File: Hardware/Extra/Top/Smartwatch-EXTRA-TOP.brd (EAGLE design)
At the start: 38 x 38 mm, 69 parts, among them SW6 SWITCH.MOM, SW7 SWITCH.MOM, U2 NRF52832_MODULE_MDBT42, U4 FT231XS, U5 PHOTOTRANSISTOR

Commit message: Extra features updated
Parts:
- removed C25: 1u, LinnesLab-Passives:C0603
- removed C26: 100n, LinnesLab-Passives:C0603
- removed D4: (no value), LinnesLab-DiscreteSemi:USC
- removed LED5: RED, LinnesLab-LED:LED-0603
- removed LED6: YELLOW, LinnesLab-LED:LED-0603
- removed Q1: (no value), LinnesLab-DiscreteSemi:SOT23-3
- removed R17: 1k, LinnesLab-Passives:R0603
- removed SW6, SW7: SWITCH.MOM, LinnesLab-Switches:TACTILE_SWITCH_SMD_6.2MM_TALL
- removed U4: FT231XS, LinnesLab-DigitalIC:SSOP20_L
- added C2: 10u, LinnesLab-Passives:C0805
- added C27: 10p, LinnesLab-Passives:C0603
- added C28: 1u, LinnesLab-Passives:C0603
- added C29: 100n, LinnesLab-Passives:C0603
- added D3: (no value), LinnesLab-DiscreteSemi:USC
- added J3: (no value), LinnesLab-Connectors:1X04_1.27MM
- added LED1: RED, LinnesLab-LED:LED-0603
- added LED2: BLUE, LinnesLab-LED:LED-0603
- added MIC1: (no value), LinnesLab-Electromechanical:MICROPHONE_CMEJ-0415-42-P
- added Q2: (no value), LinnesLab-DiscreteSemi:SOT23-3@1
- added Q3: (no value), LinnesLab-DiscreteSemi:SOT23-3
- added R21: 100k, LinnesLab-Passives:R0603
- added R22, R23, R26: 10k, LinnesLab-Passives:R0603
- added R9: 27, LinnesLab-Passives:R0603
- added U1: NRF52832_MODULE_MDBT42, LinnesLab-Microcontrollers:BLE_MODULE_RAYTAC_MDBT42
- added U6: MCP9808-MSOP8, LinnesLab-Sensors:MSOP08
- C1: value 4.7u -> 1u
- C10, C11: value 300p -> 2.2uF; device LinnesLab-Passives:C0603 -> LinnesLab-Passives:C0402
- C12: value 10u -> 2.2uF; device LinnesLab-Passives:C0805 -> LinnesLab-Passives:C0402
- C13, C18: value 2.2uF -> 100n; device LinnesLab-Passives:C0402 -> LinnesLab-Passives:C0603
- C14: value 100n -> 4.7u
- C15, C17: value 2.2uF -> 47p; device LinnesLab-Passives:C0402 -> LinnesLab-Passives:C0603
- C16: value 10uF -> 1u
- C19: value 2.2uF -> 1u; device LinnesLab-Passives:C0402 -> LinnesLab-Passives:C0603
- C20: value 2.2u -> 4.7u
- C22: value 47p -> 2.2u
- C23: value 47p -> 100n
- C24: value 10p -> 100n
- C3: value 4.7u -> (none)
- C4: value 100n -> (none)
- C5, C6: value 1u -> 300p
- C7: value 1u -> 10uF
- C8, C9: value (none) -> 2.2uF; device LinnesLab-Passives:C0603 -> LinnesLab-Passives:C0402
- J1: device LinnesLab-Connectors:1X07 -> LinnesLab-Connectors:1X07_1.27MM
- LED4: value BLUE -> YELLOW
- R11: value (none) -> 4.7k
- R15: value 10k -> 1k
- R16: value 27 -> 1k
- R18: value 1k -> 10k
- R6: value 10k -> 390k
- R7: value 390k -> 10k
- U2: value NRF52832_MODULE_MDBT42 -> (none); device LinnesLab-Microcontrollers:BLE_MODULE_RAYTAC_MDBT42 -> LinnesLab-Displays:UG-2864HSWEG01_0.96IN_NO-WRAPAROUND
- U3: value (none) -> FT231XS; device LinnesLab-Displays:UG-2864HSWEG01_0.96IN_NO-WRAPAROUND -> LinnesLab-DigitalIC:SSOP20_L
- moved R19 35.7 mm to (35.6, 8.17)
- moved LED4 35.1 mm to (4.55, 4.29)
- moved C11 33.2 mm to (2.93, 2.28), turned to 90 degrees
- moved U5 32.2 mm to (28.2, 7.97), turned to 270 degrees
- moved C12 29.9 mm to (1.61, 2.30)
- moved R8 28.9 mm to (2.64, 22.0), turned to 0 degrees
- moved C22 28.0 mm to (31.9, 8.10), turned to 90 degrees
- moved C5 27.7 mm to (30.9, 13.1)
- moved C19 27.6 mm to (5.81, 29.8)
- moved C14 27.1 mm to (6.17, 17.5), turned to 90 degrees
- moved C16 26.2 mm to (5.95, 25.1), turned to 270 degrees
- moved C13 24.1 mm to (33.8, 13.4), turned to 0 degrees
- moved D5 23.7 mm to (30.4, 9.48), turned to 0 degrees
- moved R18 23.6 mm to (30.2, 7.99), turned to 270 degrees
- moved C3 22.9 mm to (25.7, 15.9), turned to 180 degrees
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- renumbered CHRG2 to CHRG1, CORTEX1 to DEBUG1, JP2 to JP1, L2 to L1, LDO2 to LDO1, SW3 to SW1, USB2 to USB1, XTAL2 to XTAL1
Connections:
- removed net A0/LIGHT: C20.1, R19.2, U2.15, U5.2
- removed net D11/SW1: SW7.A1, U2.25
- removed net D15/SW2: SW6.A1, U2.29
- removed net D29/LED.CTRL: J1.6, U2.6
- removed net D5/MOTOR: Q1.1, R15.2, U2.18
- removed net N$21: SW7.B1, SW7.B2
- removed net N$22: SW6.B1, SW6.B2
- new net A0/MICROPHONE: Q2.3, R21.2, R22.1, U1.15
- new net A5/LIGHT: C22.1, R18.2, U1.6, U5.2
- new net ALERT: R26.1, U6.3
- new net D11/MOTOR: Q3.1, R19.2, U1.25
- new net D15/LED.CTRL: J1.6, U1.29
- new net D5/CD1: U1.18
- new net N$19: C23.1, MIC1.+, R23.1
- new net N$20: C23.2, Q2.1, R21.1
- net !CTS: now also U3.9; no longer U4.9
- net !DTR: now also U3.1; no longer U4.1
- net 3.3V: now also C11.2, C18.2, C19.1, C2.2, C24.1, C27.2, C28.1, C29.1, D5.-, J3.2, LED3.A, LED4.A, R12.2, R22.2, R23.2, R26.2, R7.2, U1.11, U2.6, U2.9, U3.14, U3.3, U6.8; no longer C17.2, C19.2, C24.2, C25.1, C26.1, C4.2, C6.1, D2.-, LED5.A, LED6.A, R5.2, R8.2, U2.11, U3.6, U3.9, U4.14, U4.3
- net A4/BATT: now also U1.5; no longer U2.5
- net A6/TIA: now also U1.7; no longer U2.7
- net A7/PPG: now also U1.8; no longer U2.8
- net D16/CS.OLED: now also U1.30, U2.13; no longer U2.30, U3.13
- net D27/CHRG.STAT: now also R8.1, U1.4; no longer R12.1, U2.4
- net D3/RESET.OLED: now also U1.16, U2.14; no longer U2.16, U3.14
- net D4/DC.OLED: now also U1.17, U2.15; no longer U2.17, U3.15
- net D7/SD.CS: now also U1.20; no longer U2.20
- net DFU: now also U1.34; no longer U2.34
- net DTR: now also C13.1; no longer C14.1
- net FRST: now also U1.38; no longer U2.38
- net FT3V3: now also U3.13; no longer U4.13
- net GND: now also C1.2, C11.1, C14.1, C15.1, C17.2, C19.2, C2.1, C24.2, C28.2, C29.2, C3.1, C4.2, C5.2, C7.1, C9.1, J3.1, LED1.C, LED2.C, MIC1.-, Q2.2, Q3.2, R12.1, R18.1, R5.1, R6.2, U1.1, U1.12, U1.24, U1.39, U2.10, U2.29, U2.30, U2.8, U3.16, U3.6, U6.4, U6.5, U6.6, U6.7; no longer C1.1, C10.2, C11.2, C17.1, C19.1, C23.1, C25.2, C26.2, C3.2, C4.1, C5.1, C7.2, C8.1, C9.2, LED3.C, LED4.C, Q1.2, R15.1, R6.1, R7.2, R8.1, U2.24, U2.39, U3.1, U3.10, U3.12, U3.29, U3.30, U3.8, U4.16, U4.6
- net LED1: now also U1.31; no longer U2.31
- net LED2: now also U1.33; no longer U2.33
- net MISO: now also U1.28; no longer U2.28
- net MOSI: now also U1.27, U2.19; no longer U2.27, U3.19
- net N$1: now also R5.2, U2.11; no longer R6.2, U3.11
- net N$10: now also LED2.A; no longer LED4.A
- net N$11: now also U1.10; no longer U2.10
- net N$12: now also C1.1, U1.9; no longer C7.1, U2.9
- net N$13: now also C7.2, U2.28; no longer C16.2, U3.28
- net N$15: now also C9.2, U2.27; no longer C18.2, U3.27
- net N$18: now also C27.1, D5.+, Q3.3; no longer C24.1, D2.+, Q1.3
- net N$2: now also R6.1, U2.26; no longer R7.1, U3.26
- net N$25: now also R9.2, U3.12; no longer R10.2, U4.12
- net N$26: now also R10.2, U3.11; no longer R16.2, U4.11
- net N$27: now also LED3.C, R15.2; no longer LED5.C, R17.2
- net N$28: now also LED4.C, R16.2; no longer LED6.C, R18.2
- net N$3: now also C10.2, U2.2; no longer C13.2, U3.2
- net N$4: now also C3.2, U1.13; no longer C8.2, U2.13
- net N$5: now also C10.1, U2.3; no longer C13.1, U3.3
- net N$6: now also C4.1, U1.14; no longer C9.1, U2.14
- net N$7: now also C8.2, U2.4; no longer C15.2, U3.4
- net N$8: now also C8.1, U2.5; no longer C15.1, U3.5
- net N$9: now also LED1.A; no longer LED3.A
- net P0.09/NFC1: now also C5.1, U1.22; no longer C11.1, U2.22
- net P0.10/NFC2: now also C6.1, U1.23; no longer C10.1, U2.23
- net RESET: now also C13.2, R7.1, U1.35; no longer C14.2, R5.1, U2.35
- net RXD: now also U1.21, U3.4; no longer U2.21, U4.4
- net RXLED: now also R15.1, U3.17; no longer R17.1, U4.17
- net SCK: now also U1.26, U2.18; no longer U2.26, U3.18
- net SCL: now also J3.3, U1.3, U6.2; no longer U2.3
- net SDA: now also J3.4, U1.2, U6.1; no longer U2.2
- net SWCLK: now also U1.36; no longer U2.36
- net SWDIO: now also U1.37; no longer U2.37
- net SWO: now also U1.32; no longer U2.32
- net TXD: now also U1.19, U3.20; no longer U2.19, U4.20
- net TXLED: now also R16.1, U3.10; no longer R18.1, U4.10
- net USB+: now also C17.1, R10.1; no longer C22.1, R16.1
- net USB-: now also C15.2, R9.1; no longer C23.2, R10.1
- net VIN: now also C14.2, C16.2, D2.-, D3.-, R8.2; no longer C1.2, C5.2, D4.-, D5.-, R12.2
- net VLIPO: now also C20.1, D2.+; no longer C3.1, D4.+
- net V_USB: now also D3.+, U3.15; no longer D5.+, U4.15
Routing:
- net A0/LIGHT: track 39.4 -> 0.00 mm, vias 2 -> 0
- net A0/MICROPHONE: track 0.00 -> 37.3 mm, vias 0 -> 2
- net A5/LIGHT: track 0.00 -> 37.2 mm, vias 0 -> 2
- net SCL: track 17.2 -> 48.2 mm, vias 0 -> 2
- net SDA: track 21.2 -> 49.5 mm, vias 0 -> 5
- net D15/LED.CTRL: track 0.00 -> 25.5 mm, vias 0 -> 2
- net D15/SW2: track 24.4 -> 0.00 mm, vias 2 -> 0
- net D11/SW1: track 23.0 -> 0.00 mm, vias 2 -> 0
- net D5/MOTOR: track 18.9 -> 0.00 mm, vias 2 -> 0
- net D11/MOTOR: track 0.00 -> 17.0 mm, vias 0 -> 1
- net D29/LED.CTRL: track 11.0 -> 0.00 mm
- net N$22: track 7.95 -> 0.00 mm
- net N$21: track 7.95 -> 0.00 mm
- net A6/TIA: track 16.5 -> 23.7 mm, vias 0 -> 2
- net GND: track 93.4 -> 86.2 mm, vias 30 -> 32
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
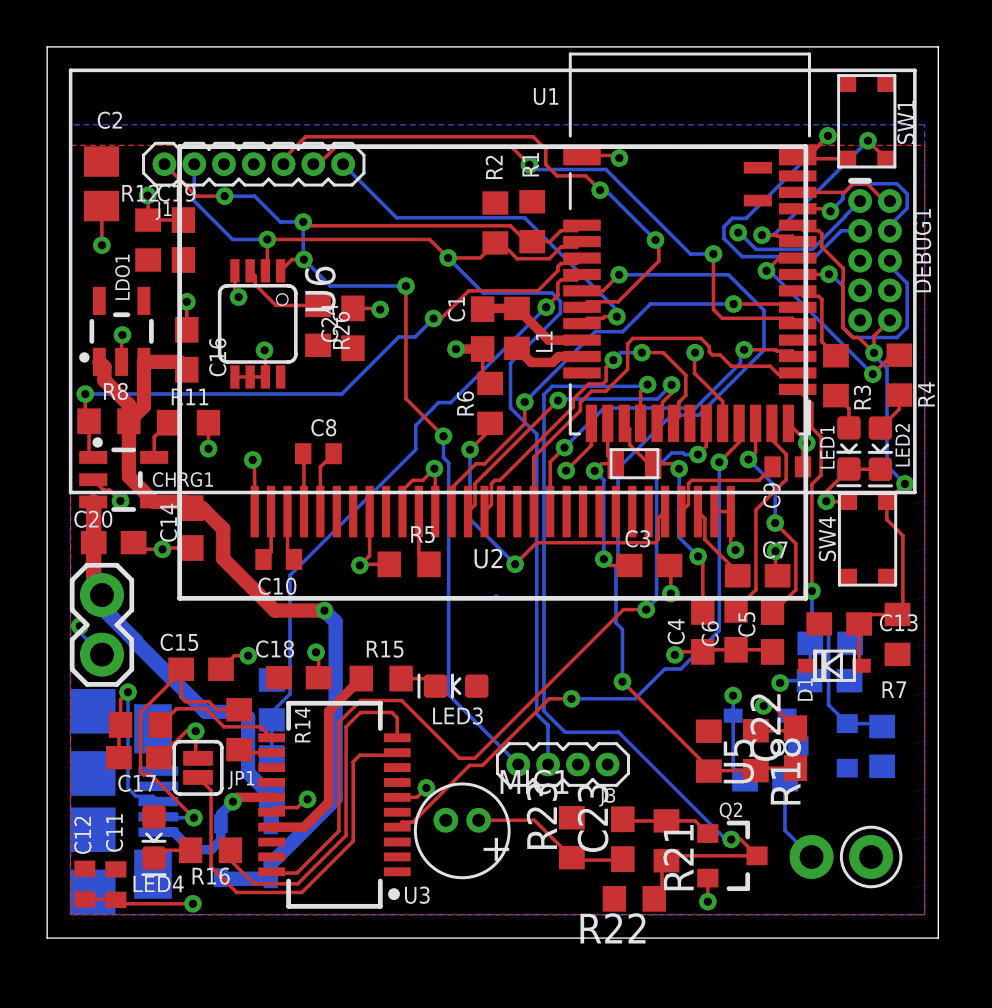
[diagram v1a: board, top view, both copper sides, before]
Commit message: Extra Silkscreens updated
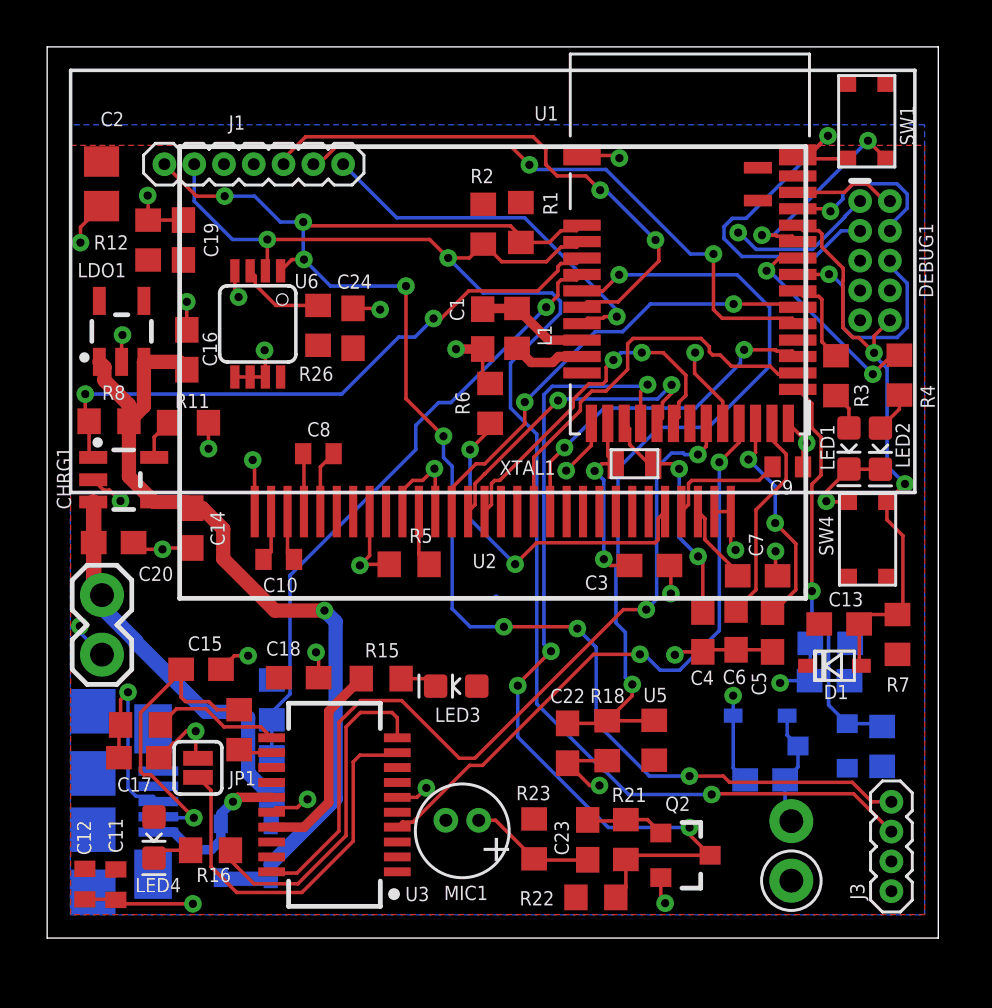
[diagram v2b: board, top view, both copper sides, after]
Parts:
- moved J3 13.3 mm to (36.0, 2.00), turned to 90 degrees
- moved C22 9.72 mm to (22.2, 8.31), turned to 270 degrees
- moved R18 6.35 mm to (23.9, 8.41), turned to 90 degrees
- moved U5 2.38 mm to (25.9, 8.43), turned to 90 degrees
- moved M1 2.15 mm to (31.7, 3.72), turned to 90 degrees
- moved Q2 2.00 mm to (27.2, 3.53)
- moved R21 1.74 mm to (24.7, 4.20)
- moved R22 1.64 mm to (23.4, 1.73)
- moved R23 1.61 mm to (20.8, 4.23)
- moved C23 1.50 mm to (23.1, 4.19)
- moved R2 0.52 mm to (18.6, 30.4)
- moved R1 0.48 mm to (20.2, 30.5)
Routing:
- net SDA: track 49.5 -> 65.9 mm, vias 5 -> 8
- net SCL: track 48.2 -> 62.9 mm, vias 2 -> 3
- net A5/LIGHT: track 37.2 -> 34.9 mm
- net N$18: track 6.92 -> 5.03 mm
- net N$19: track 6.95 -> 5.38 mm
- net RXD: track 26.4 -> 27.0 mm
- net A0/MICROPHONE: track 37.3 -> 37.6 mm, vias 2 -> 4

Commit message: Microphone Removed,Silkscreen Updated, Bom Updated
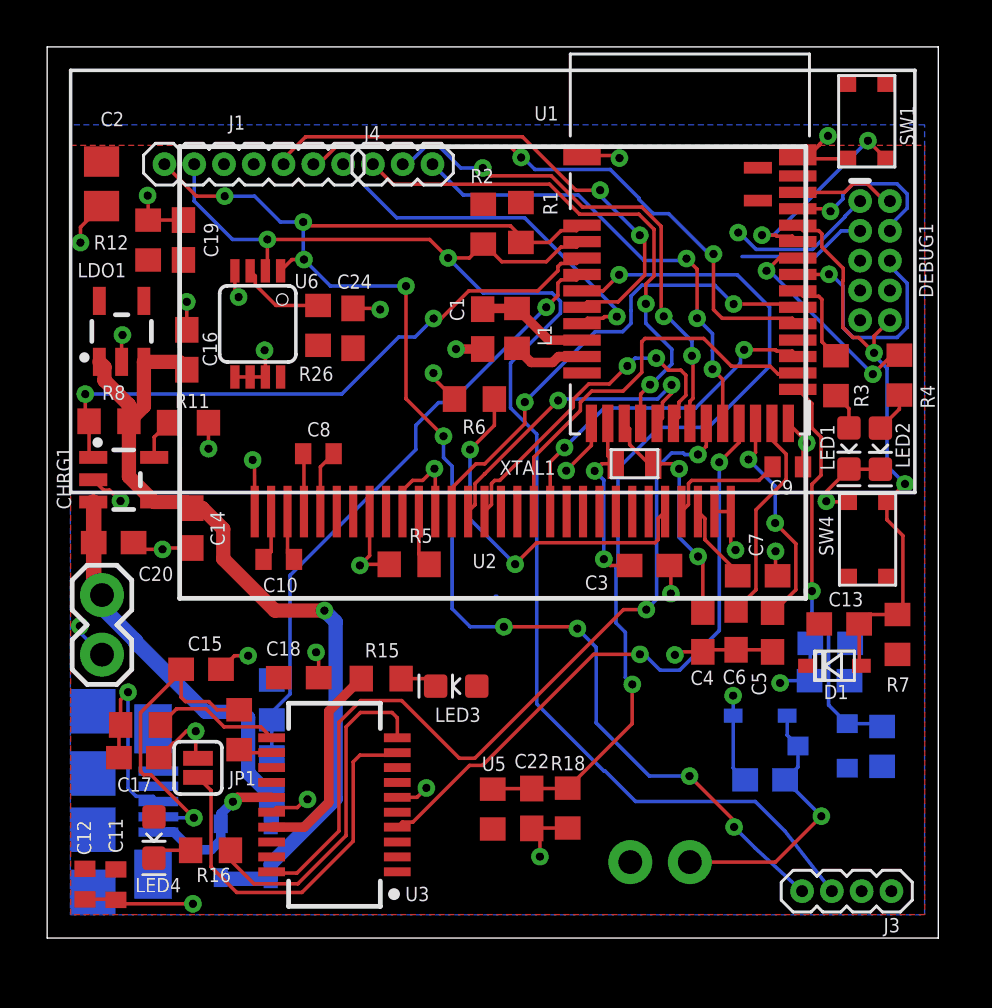
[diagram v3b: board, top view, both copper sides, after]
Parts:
- removed C23: 100n, LinnesLab-Passives:C0603
- removed MIC1: (no value), LinnesLab-Electromechanical:MICROPHONE_CMEJ-0415-42-P
- removed Q2: (no value), LinnesLab-DiscreteSemi:SOT23-3@1
- removed R21: 100k, LinnesLab-Passives:R0603
- removed R22, R23: 10k, LinnesLab-Passives:R0603
- added J4: (no value), LinnesLab-Connectors:1X03_1.27MM
- moved U5 7.49 mm to (19.0, 5.50)
- moved M1 5.62 mm to (26.1, 3.24), flipped to the bottom, turned to 180 degrees
- moved R18 3.33 mm to (22.2, 5.54)
- moved C22 3.17 mm to (20.7, 5.53)
- moved R6 0.69 mm to (18.2, 23.0), turned to 180 degrees
- turned J3 to 180 degrees
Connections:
- removed net A0/MICROPHONE: Q2.3, R21.2, R22.1, U1.15
- removed net D5/CD1: U1.18
- removed net D7/SD.CS: U1.20
- removed net N$19: C23.1, MIC1.+, R23.1
- removed net N$20: C23.2, Q2.1, R21.1
- new net A.IN: J4.1, U1.15
- new net B.IN: J4.3, U1.20
- new net MOM.BUTTON: J4.2, U1.18
- net 3.3V: no longer R22.2, R23.2
- net GND: no longer MIC1.-, Q2.2
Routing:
- net A0/MICROPHONE: track 37.6 -> 0.00 mm, vias 4 -> 0
- net A.IN: track 0.00 -> 22.6 mm, vias 0 -> 2
- net MOM.BUTTON: track 0.00 -> 21.8 mm, vias 0 -> 3
- net B.IN: track 0.00 -> 20.2 mm, vias 0 -> 3
- net GND: track 86.6 -> 77.1 mm
- net N$18: track 5.03 -> 11.8 mm, vias 0 -> 1
- net N$19: track 5.38 -> 0.00 mm
- net D7/SD.CS: track 3.52 -> 0.00 mm, vias 1 -> 0
- net N$20: track 3.39 -> 0.00 mm
- net A5/LIGHT: track 34.9 -> 38.0 mm
- net SDA: track 65.9 -> 63.8 mm, vias 8 -> 9
- net D16/CS.OLED: track 19.6 -> 21.0 mm
- net SCL: track 62.9 -> 61.5 mm, vias 3 -> 2
- net N$2: track 15.0 -> 16.1 mm
- net A6/TIA: track 23.7 -> 22.7 mm
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
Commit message: BOMs finished
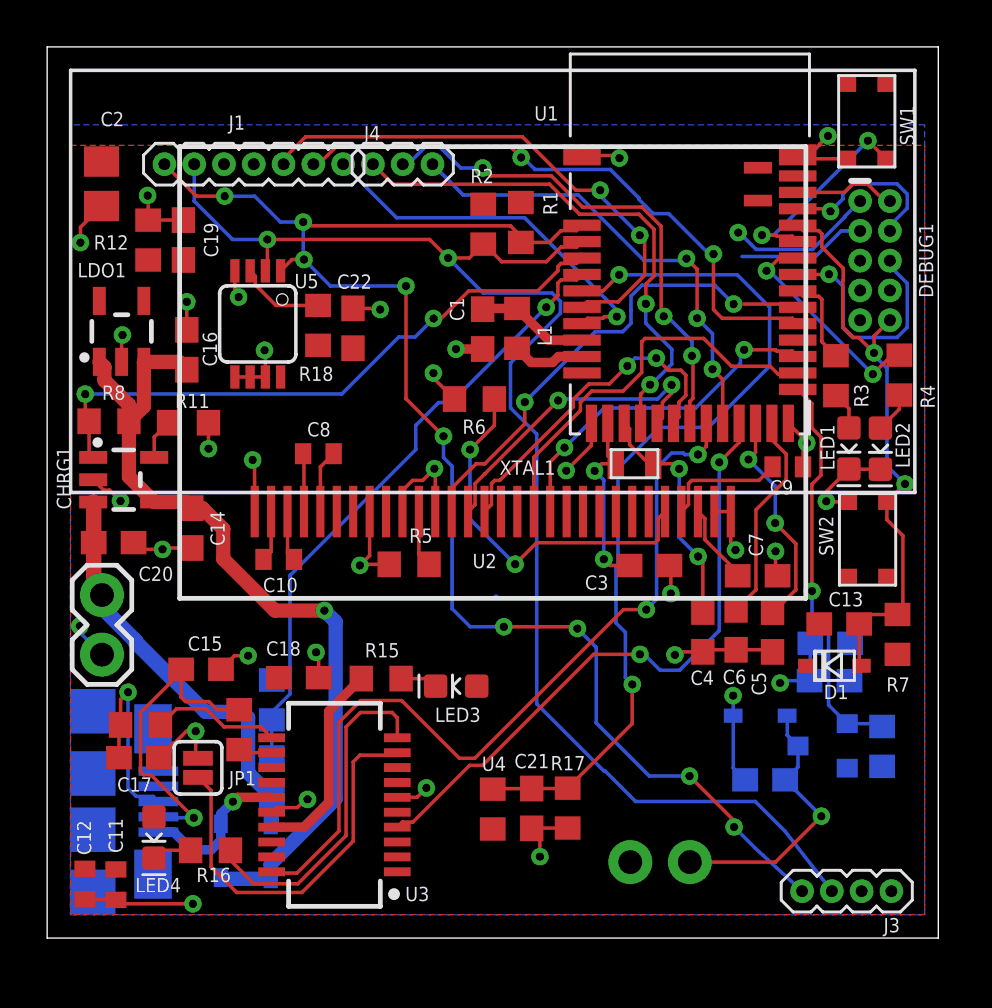
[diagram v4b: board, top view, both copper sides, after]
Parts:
- removed C28: 1u, LinnesLab-Passives:C0603
- removed R26: 10k, LinnesLab-Passives:R0603
- removed U6: MCP9808-MSOP8, LinnesLab-Sensors:MSOP08
- added C21: 2.2u, LinnesLab-Passives:C0603
- added R17: 10k, LinnesLab-Passives:R0603
- added U4: PHOTOTRANSISTOR, LinnesLab-Sensors:R0603
- C22: value 2.2u -> 100n
- C24: value 100n -> 1u
- C3, C4: value (none) -> 12 pF
- U5: value PHOTOTRANSISTOR -> MCP9808-MSOP8; device LinnesLab-Sensors:R0603 -> LinnesLab-Sensors:MSOP08
- moved C24 25.3 mm to (33.4, 11.0), flipped to the bottom, turned to 180 degrees
- moved R18 23.2 mm to (11.6, 26.1), turned to 270 degrees
- moved U5 23.0 mm to (8.98, 26.2), turned to 180 degrees
- moved C22 21.8 mm to (13.0, 26.0), turned to 90 degrees
- renumbered C27 to C23, C29 to C25, D5 to D4, Q3 to Q1, SW4 to SW2
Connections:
- net 3.3V: now also C22.1, R18.2, U4.1, U5.8; no longer C28.1, R26.2, U5.1, U6.8
- net A5/LIGHT: now also C21.1, R17.2, U4.2; no longer C22.1, R18.2, U5.2
- net ALERT: now also R18.1, U5.3; no longer R26.1, U6.3
- net GND: now also C21.2, R17.1, U5.4, U5.5, U5.6, U5.7; no longer C28.2, R18.1, U6.4, U6.5, U6.6, U6.7
- net SCL: now also U5.2; no longer U6.2
- net SDA: now also U5.1; no longer U6.1
